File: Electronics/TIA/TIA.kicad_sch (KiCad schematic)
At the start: 7 parts

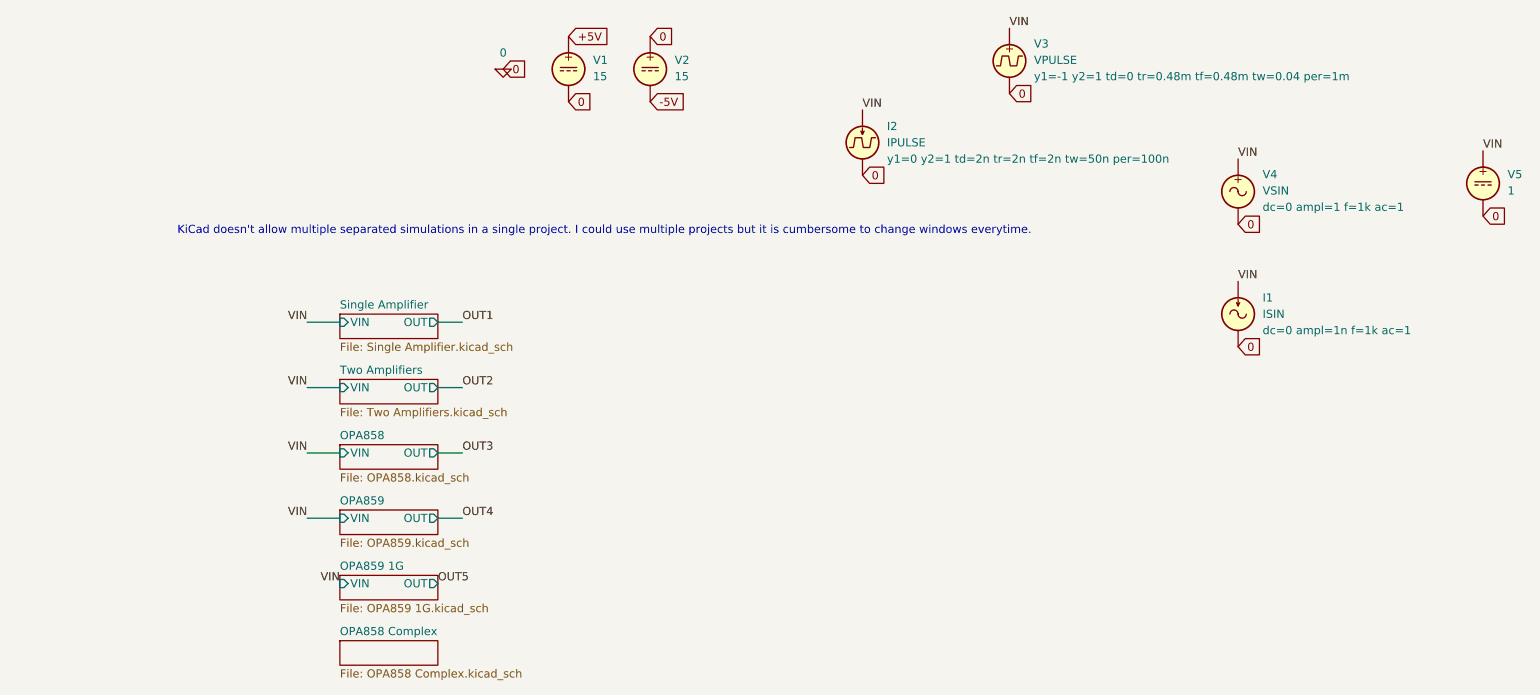
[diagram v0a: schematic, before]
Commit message: Remove old simulations
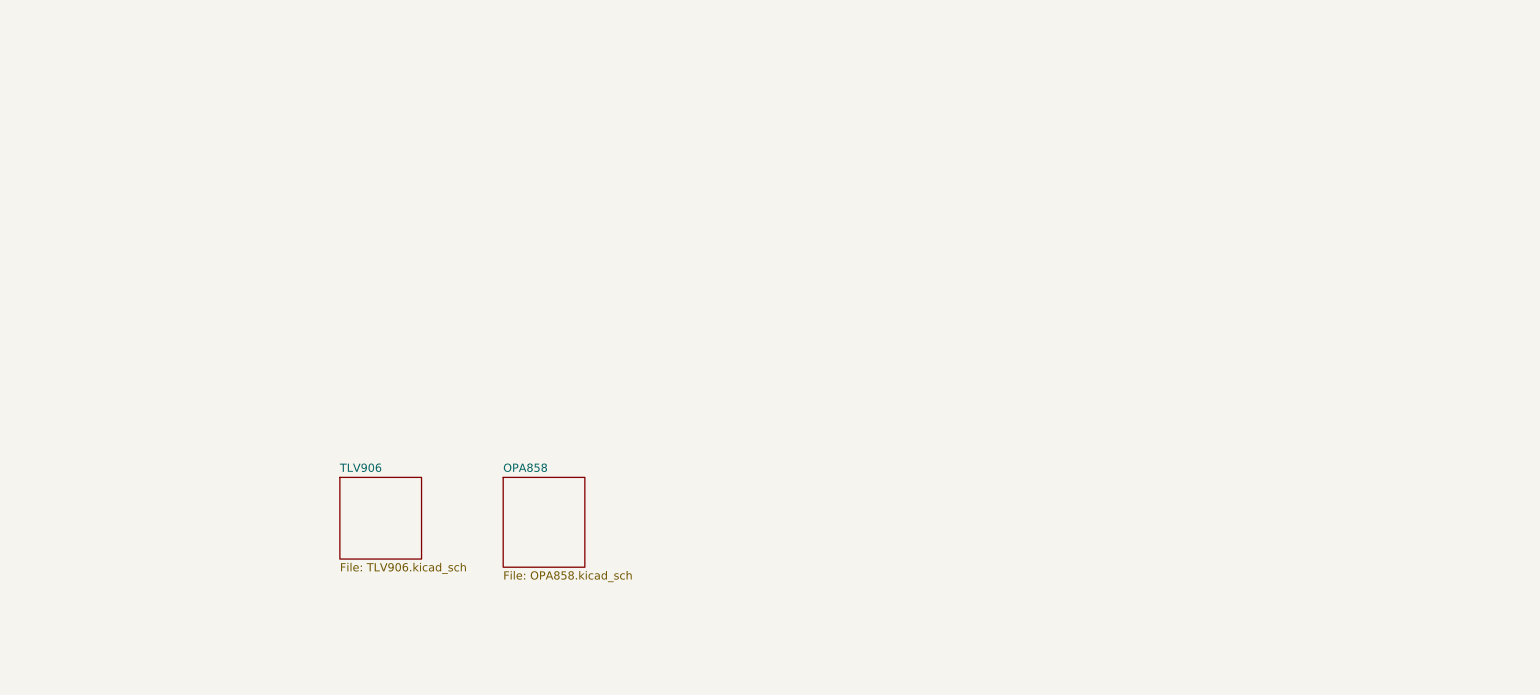
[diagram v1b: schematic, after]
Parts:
- removed I1: ISIN, symbol Simulation_SPICE:ISIN
- removed I2: IPULSE, symbol Simulation_SPICE:IPULSE
- removed V1, V2: 15, symbol Simulation_SPICE:VDC
- removed V3: VPULSE, symbol Simulation_SPICE:VPULSE
- removed V4: VSIN, symbol Simulation_SPICE:VSIN
- removed V5: 1, symbol Simulation_SPICE:VDC
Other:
- removed sheet OPA858 Complex
- removed sheet OPA859
- removed sheet OPA859 1G
- removed sheet Single Amplifier
- removed sheet Two Amplifiers
- added sheet TLV906 (TLV906.kicad_sch)
- sheet OPA858 ports: added none; removed OUT, VIN
- note removed: "KiCad doesn't allow multiple separated simulations in a single project. I could use multiple projects but it is cumbersome to change windows everytime."

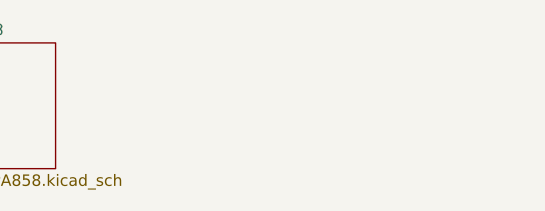
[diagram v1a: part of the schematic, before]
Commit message: Create simulation for RS8751
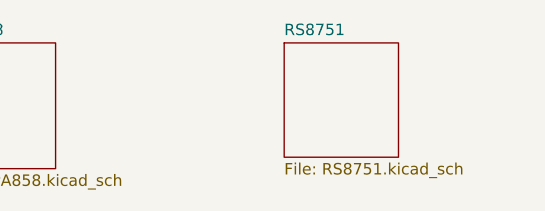
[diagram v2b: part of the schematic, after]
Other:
- added sheet RS8751 (RS8751.kicad_sch)
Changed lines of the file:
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@@
 	(paper "A4")
+	(sheet
+		(at 114.3 88.9)
+		(size 12.7 12.7)
+		(exclude_from_sim no)
+		(in_bom yes)
+		(on_board yes)
+		(dnp no)
+		(fields_autoplaced yes)
+		(stroke
+			(width 0.1524)
+			(type solid)
+		)
+		(fill
+			(color 0 0 0 0.0000)
+		)
+		(property "Sheetname" "RS8751"
+			(at 114.3 88.1884 0)
+			(effects
+				(font
+					(size 1.27 1.27)
+				)
+				(justify left bottom)
+			)
+		)
+		(property "Sheetfile" "RS8751.kicad_sch"
+			(at 114.3 102.1846 0)
+			(effects
+				(font
+					(size 1.27 1.27)
+				)
+				(justify left top)
+			)
+		)
+		(instances
+			(project "TIA"
+				(path "/71573f97-d585-4d55-ac00-8cb3ed311569"
+					(page "7")
+				)
+			)
+		)
+	)
 	(sheet
 		(at 76.2 88.9)
 		(size 12.7 13.97)
-		(exclude_from_sim no)
+		(exclude_from_sim yes)
 		(in_bom yes)
 		(on_board yes)
